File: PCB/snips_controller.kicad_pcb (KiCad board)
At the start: 4 copper layers, 35 x 99.9 mm, 95 parts

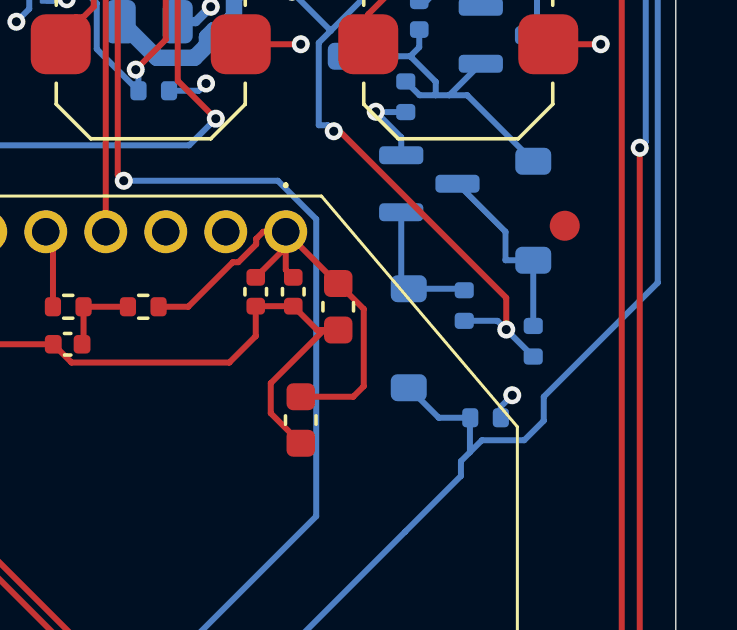
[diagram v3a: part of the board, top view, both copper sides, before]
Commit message: fix: make every BOM Value unambiguous for the fab, and switch D_INV_ISO1 to SOT-323 (#61)
* fix: make every BOM Value unambiguous for the fab, and switch D_INV_ISO1 to SOT-323

PCBWay flagged D_INV_ISO1: "BAT54W" is SOT-323 from nearly every maker, but we
had picked Yangjie's SOD-123 variant. A fab only sees Designator, Footprint,
Quantity and Value in the BOM (never MF/MPN/LCSC), so a bare part name is
ambiguous. Fixes the class of problem, not just this part:

- Every component's Value is now "<label> | <MPN> | <manufacturer> | <package>"
  (label dropped when it repeats the MPN; commas/periods stripped so the CSV
  never needs quoting). BT1 keeps its RIGHT-ANGLE HORIZONTAL note. Applied to
  all 81 parts across every sheet and the PCB.
- scripts/bom_values.py builds, applies, and checks these values, including
  that the PCB copy of Value/MF/MPN/footprint matches the schematic. New
  footprints must be added to its package table on purpose; hand-sourced parts
  with no MPN (J_STICK1) are listed explicitly.
- D_INV_ISO1 -> Diodes BAT54W-7-F in SOT-323 (common part, several makers).
  Pin 1 anode / pin 2 not connected / pin 3 cathode, confirmed against
  Nexperia's numbered pinning table and Diodes' datasheet. Uses KiCad's
  Diode:BAT54W symbol; PCB footprint replaced and rerouted. Electrically the
  same BAT54 family (30V, 200mA, 2uA leakage at 25V), so the SPICE model and
  scripts/spice/latch_sim.py still pass.
- Layout diagrams now say AO3401A for Q_PWR1 (they were stale since it was
  swapped from DMG2305UX) and BAT54W-7-F/SOT-323 for D_INV_ISO1.
- Repo CLAUDE.md documents the Value rule and the script.

ERC/DRC clean; production files regenerated.

Co-Authored-By: Claude Sonnet 5 <noreply@anthropic.com>

* chore: commit KiCad project settings (reordered used-designators list)

Co-Authored-By: Claude Sonnet 5 <noreply@anthropic.com>

---------

Co-authored-by: Claude Sonnet 5 <noreply@anthropic.com>
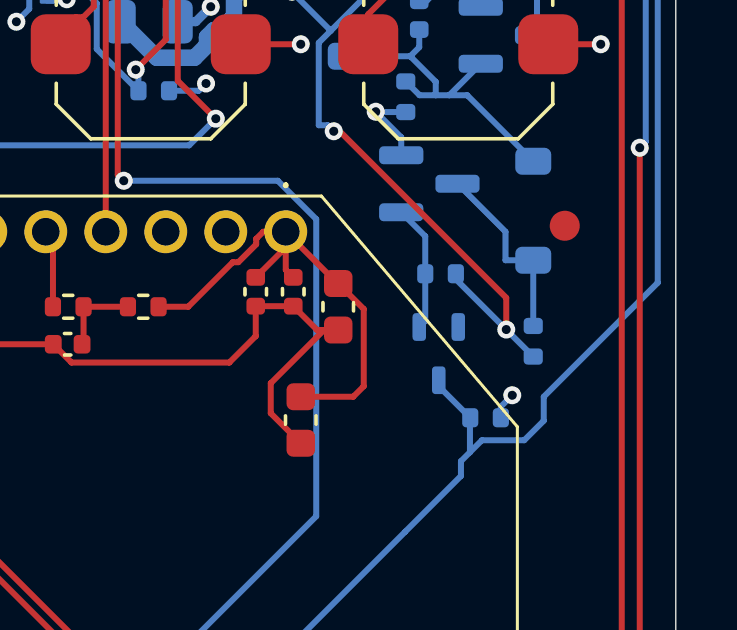
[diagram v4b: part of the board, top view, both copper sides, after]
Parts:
- BT1: value JST-PH_2Pin_Battery_RightAngle_Horizontal -> PH 2-pin battery RIGHT-ANGLE HORIZONTAL | S2B-PH-K(LF)(SN) | JST | THT right-angle horizontal 2.00mm
- C_3V3_1, C_XBEE_VCC4: value 10µF -> 10µF | CL10A106KP8NNNC | Samsung Electro-Mechanics | 0603
- C_3V3_2, C_DBNC1, C_HALL1, C_LATCH_G1, C_OLED_2, C_RGB1, C_STICK1, C_SYS_2, C_VIN_2, C_XBEE_RC1, C_XBEE_VCC1: value 100nF -> 100nF | CL05B104KO5NNNC | Samsung Electro-Mechanics | 0402
- C_3V3_3: value 39pF -> 39pF | CC0402JRNPO9BN390 | Yageo | 0402
- C_ACCEL_1: value 10nF -> 10nF | CL05B103KB5NNNC | Samsung Electro-Mechanics | 0402
- C_ACCEL_2: value 100pF -> 100pF | 0402CG101J500NT | FH (Guangdong Fenghua Advanced Tech) | 0402
- C_ACCEL_3: value 2.2nF -> 2.2nF | CL05B222KB5NNNC | Samsung Electro-Mechanics | 0402
- C_BAT1, C_BUCK_IN1, C_OLED_1, C_SYS_1, C_VIN_1: value 10µF -> 10µF | CL21A106KAYNNNE | Samsung Electro-Mechanics | 0805
- C_BUCK_OUT1: value 22µF -> 22µF | CL21A226MAQNNNE | Samsung Electro-Mechanics | 0805
- C_XBEE_VCC2: value 1µF -> 1µF | CL10A105KB8NNNC | Samsung Electro-Mechanics | 0603
- C_XBEE_VCC3: value 47pF -> 47pF | 0402CG470J500NT | FH (Guangdong Fenghua Advanced Tech) | 0402
- D_INV_ISO1: value BAT54W -> BAT54W-7-F | Diodes Incorporated | SOT-323 (SC-70); footprint Diode_SMD:D_SOD-123 -> Package_TO_SOT_SMD:SOT-323_SC-70
- D_OR1, D_OR2: value 1N4148W -> 1N4148W | ST(Semtech) | SOD-123
- D_RGB1: value SK6812MINI-E-012 -> SK6812MINI-E-012 | SK6812MINI-E | OPSCO Optoelectronics | SMD 3.2x2.8mm
- D_VBUS_TVS1: value PESD5V0S1BA -> TPPESD5V0S1BA | TECH PUBLIC | SOD-323
- J_USB1: value USB-C -> USB-C | TYPE-C-31-M-12 | Hroparts Elec | USB-C receptacle
- L_BUCK1: value 2.2µH -> 2.2µH | SRN4018-2R2M | Bourns | 4.0x4.0mm SMD
- Q_INV1: value MMBT3904 -> MMBT3904(RANGE:100-300) | Jiangsu Changjing Electronics Technology Co Ltd | SOT-23
- Q_LATCH1: value AO3400A -> AO3400A | Alpha & Omega Semicon | SOT-23
- Q_PWR1: value AO3401A -> AO3401A | Alpha & Omega Semicon | SOT-23
- R_BOOT_PU1, R_EN_PU1, R_STAT1, R_STAT2, R_TS1, R_XBEE_ATTN_PU1, R_XBEE_RST1: value 10kΩ -> 10kΩ | 0402WGF1002TCE | UNI-ROYAL(Uniroyal Elec) | 0402
- R_BTN_PU1, R_GATE1, R_INV_BASE1, R_INV_PU1, R_PWR_EN_PD1, R_VSYS2: value 100kΩ -> 100kΩ | 0402WGF1003TCE | UNI-ROYAL(Uniroyal Elec) | 0402
- R_CC1, R_CC2: value 5.1kΩ -> 5.1kΩ | 0402WGF5101TCE | UNI-ROYAL(Uniroyal Elec) | 0402
- R_FB1: value 255kΩ -> RC0402FR-07255KL | Yageo | 0402
- R_FB2: value 56.2kΩ -> 56.2kΩ | RC0402FR-0756K2L | Yageo | 0402
- R_ISET1: value 604Ω -> AC0402FR-07604RL | Yageo | 0402
- R_LATCH_G1: value 1MΩ -> 1MΩ | 0402WGF1004TCE | UNI-ROYAL(Uniroyal Elec) | 0402
- R_RGB1: value 470Ω -> 0402WGF4700TCE | UNI-ROYAL(Uniroyal Elec) | 0402
- R_USB_DM1, R_USB_DP1: value 27Ω -> RC0402FR-0727RL | Yageo | 0402
- R_VSET1: value 18kΩ -> RC0402FR-0718KL | Yageo | 0402
- R_VSYS1: value 200kΩ -> 200kΩ | 0402WGF2003TCE | UNI-ROYAL(Uniroyal Elec) | 0402
- R_XBEE_RC1: value 100Ω -> 0402WGF1000TCE | UNI-ROYAL(Uniroyal Elec) | 0402
- SW_BOOT1: value Panasonic_EVQP2 -> Panasonic_EVQP2 | EVQP2T02M | Panasonic | SMD tactile 2.1mm
- SW_MACRO1, SW_MACRO2, SW_MACRO3, SW_MACRO4, SW_MACRO5, SW_MACRO6: value 6x6x5mm SMD Tactile -> 6x6x5mm SMD Tactile | 1TS009A-1800-5000-CT | Hongyuan Precision | SMD tactile 6x6x5mm
- SW_PWR1, SW_THR_DN1, SW_THR_UP1, SW_TRIG_DIG1, SW_VOL_DN1, SW_VOL_UP1: value Alps_SKRTLAE010 -> SKRTLAE010 | Alps Alpine | SMD tactile horizontal
- U_ACCEL1: value QMA6100P -> QMA6100P | QST | LGA-12 2x2mm
- U_BUCK1: value TLV62569 -> TLV62569DBVR | Texas Instruments | SOT-23-5
- U_CHG1: value bq25185 -> BQ25185DLHR | Texas Instruments | WSON-10 2.2x2.0mm
- U_HALL1: value DRV5055A2 -> DRV5055A2QLPGM | Texas Instruments | TO-92 THT
- U_MCU1: value ESP32-S3-WROOM-1-N8 -> ESP32-S3-WROOM-1-N8 | Espressif Systems | SMD module 18x25.5mm
- U_OLED1: value JST-SH_4Pin_OLED -> JST-SH_4Pin_OLED | SM04B-SRSS-TB(LF)(SN) | JST | SMD horizontal 1.00mm 4-pin
- U_XBEE1: value XBee3 -> XBee3 | XB3-24Z8UT-J | Digi International | XBee through-hole
- moved R_INV_BASE1 1.32 mm to (147.2, 128.9), turned to 180 degrees
- moved D_INV_ISO1 1.12 mm to (147.1, 131.6), turned to -90 degrees
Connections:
- D_INV_ISO1 pad 1: /MCU_Core/PWR_BTN_SENSE -> /Power_Control/PWR_BTN_INV_BASE
- D_INV_ISO1 pad 2: /Power_Control/PWR_BTN_INV_BASE -> unconnected-(D_INV_ISO1-NC-Pad2)
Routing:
- net VSYS: track 85.2 -> 86.3 mm
- net /MCU_Core/PWR_BTN_SENSE: track 131.6 -> 130.8 mm
